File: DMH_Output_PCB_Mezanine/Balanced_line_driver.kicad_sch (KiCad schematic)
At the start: 40 parts, among them J31 Conn_01x06_PinHeader, J32 Conn_01x06_PinHeader, U10 NE5532, U9 NE5532

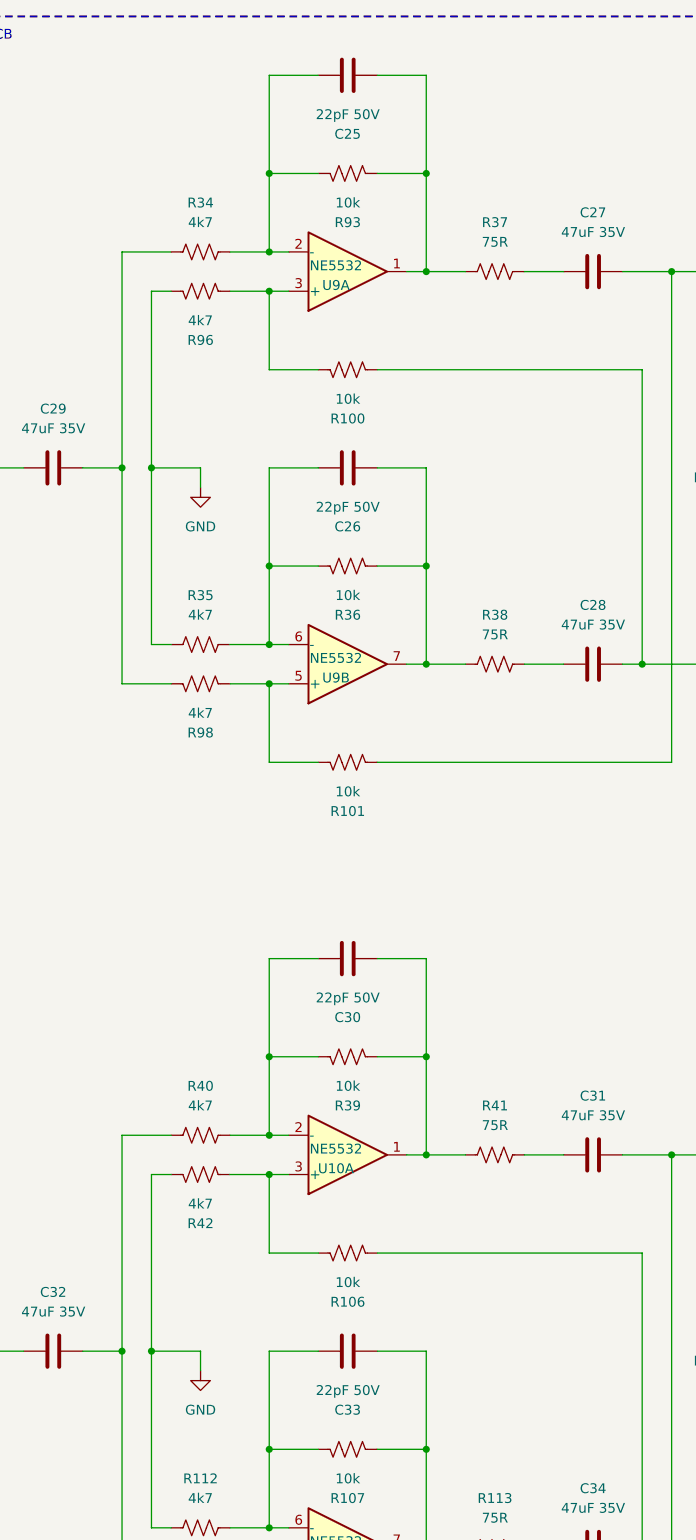
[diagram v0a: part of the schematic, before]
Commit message: Mezanine PCB comp placement done
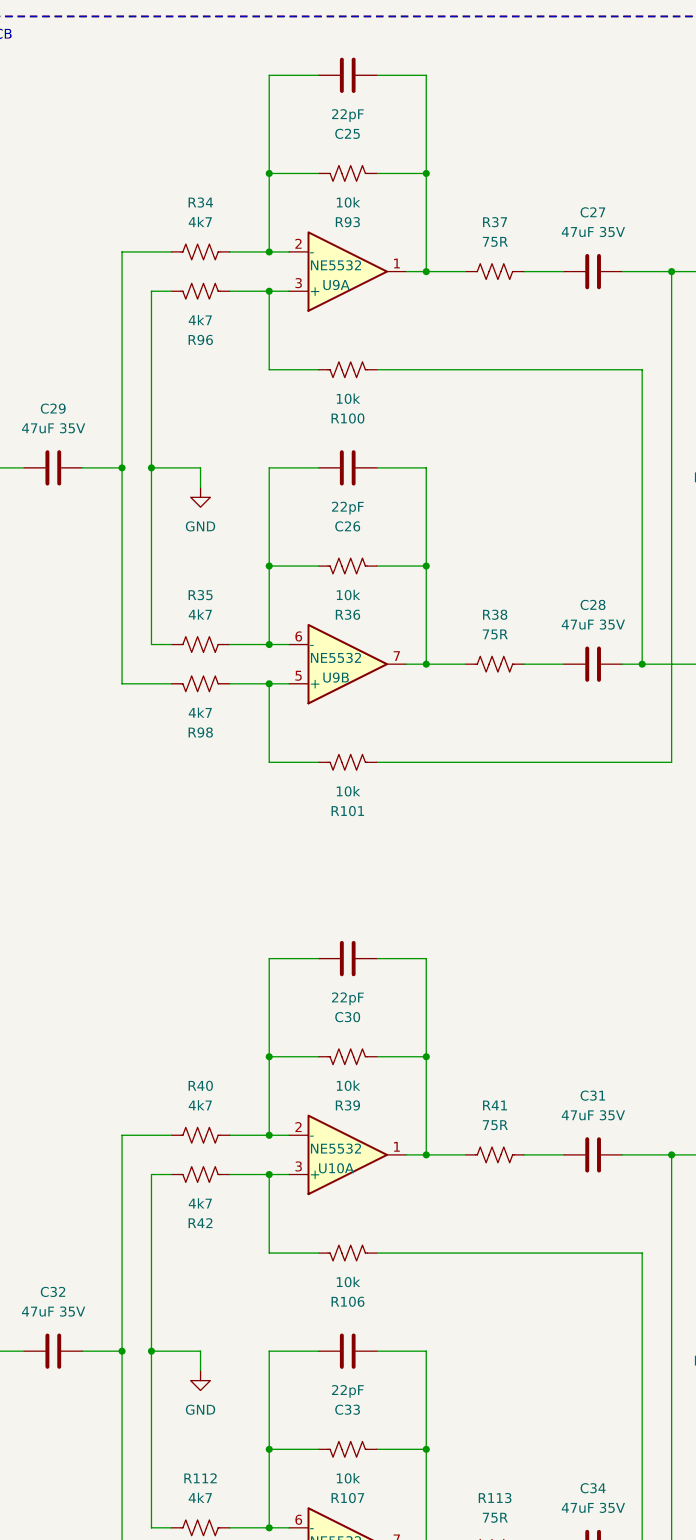
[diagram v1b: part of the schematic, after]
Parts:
- C25, C26, C30, C33: value 22pF 50V -> 22pF
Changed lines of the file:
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@@
 			)
 		)
-		(property "Value" "22pF 50V"
+		(property "Value" "22pF"
 			(at 101.6 195.58 90)
 			(show_name no)
@@
 			)
 		)
-		(property "Value" "22pF 50V"
+		(property "Value" "22pF"
 			(at 101.6 81.28 90)
 			(show_name no)
@@
 			)
 		)
-		(property "Value" "22pF 50V"
+		(property "Value" "22pF"
 			(at 101.6 144.78 90)
 			(show_name no)
@@
 			)
 		)
-		(property "Value" "22pF 50V"
+		(property "Value" "22pF"
 			(at 101.6 30.48 90)
 			(show_name no)
